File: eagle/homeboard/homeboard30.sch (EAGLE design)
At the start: 126 parts, among them IC1 XCF02S, IC2 25LC080SN, IC3 ATMEGA32U2-TQFP, Q5 BC848SMD, Q6 BC848SMD, Q7 BC848SMD, Q8 BC848SMD, T1 BSS138, T2 BC848, T3 BSS138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

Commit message: reverted changes to submitted homeboard29, moved recent changes to 29 into 30 and re-applied scart slot fix
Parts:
- C1, C3, C4, C5: value (none) -> 100nF
- C37, C38: value (none) -> 20pF
- LED1: value (none) -> 20mA
- R11, R23, R34: value (none) -> 75
- R48, R49: value (none) -> 2200
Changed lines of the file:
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@@
 <part name="Q7" library="bc548" deviceset="BC848*" device="SMD"/>
 <part name="Q8" library="bc548" deviceset="BC848*" device="SMD"/>
-<part name="R23" library="resistor" deviceset="R-EU_" device="M0805"/>
-<part name="R34" library="resistor" deviceset="R-EU_" device="M0805"/>
-<part name="C3" library="resistor" deviceset="C-EU" device="C0603"/>
-<part name="C4" library="resistor" deviceset="C-EU" device="C0603"/>
+<part name="R23" library="resistor" deviceset="R-EU_" device="M0805" value="75"/>
+<part name="R34" library="resistor" deviceset="R-EU_" device="M0805" value="75"/>
+<part name="C3" library="resistor" deviceset="C-EU" device="C0603" value="100nF"/>
+<part name="C4" library="resistor" deviceset="C-EU" device="C0603" value="100nF"/>
 <part name="U$2" library="cpcfpga" deviceset="TXO_7C" device=""/>
 <part name="REG2.5" library="cpcfpga" deviceset="NX1117" device="" value="2.5V"/>
@@
 <part name="SUPPLY5" library="supply2" deviceset="GND" device=""/>
 <part name="IC2" library="microchip" deviceset="25*" device="SN" technology="LC080"/>
-<part name="R48" library="resistor" deviceset="R-EU_" device="M0805"/>
-<part name="C1" library="resistor" deviceset="C-EU" device="C0603"/>
-<part name="C5" library="resistor" deviceset="C-EU" device="C0603"/>
-<part name="R49" library="resistor" deviceset="R-EU_" device="M0805"/>
+<part name="R48" library="resistor" deviceset="R-EU_" device="M0805" value="2200"/>
+<part name="C1" library="resistor" deviceset="C-EU" device="C0603" value="100nF"/>
+<part name="C5" library="resistor" deviceset="C-EU" device="C0603" value="100nF"/>
+<part name="R49" library="resistor" deviceset="R-EU_" device="M0805" value="2200"/>
 <part name="SUPPLY6" library="supply2" deviceset="GND" device=""/>
 <part name="SUPPLY7" library="supply2" deviceset="GND" device=""/>
@@
 <part name="SUPPLY19" library="supply2" deviceset="GND" device=""/>
 <part name="Q1" library="special" deviceset="XTAL/S" device=""/>
-<part name="C37" library="rcl" deviceset="C-EU" device="C0805"/>
-<part name="C38" library="rcl" deviceset="C-EU" device="C0805"/>
+<part name="C37" library="rcl" deviceset="C-EU" device="C0805" value="20pF"/>
+<part name="C38" library="rcl" deviceset="C-EU" device="C0805" value="20pF"/>
 <part name="SUPPLY20" library="supply2" deviceset="GND" device=""/>
 <part name="PWR_HDR" library="jumper" deviceset="JP1Q" device=""/>
@@
 <attribute name="OC_NEWARK" value="unknown"/>
 </part>
-<part name="R11" library="resistor" deviceset="R-EU_" device="M0805"/>
+<part name="R11" library="resistor" deviceset="R-EU_" device="M0805" value="75"/>
 <part name="SUPPLY17" library="supply2" deviceset="GND" device=""/>
-<part name="LED1" library="adafruit" deviceset="LED" device="CHIPLED_0805"/>
+<part name="LED1" library="adafruit" deviceset="LED" device="CHIPLED_0805" value="20mA"/>
 </parts>
 <sheets>
@@
 </segment>
 </net>
-<net name="X_CAS" class="0">
-<segment>
-<wire x1="177.8" y1="114.3" x2="162.56" y2="114.3" width="0.1524" layer="91"/>
-<label x="162.56" y="114.3" size="1.778" layer="95"/>
-</segment>
-</net>

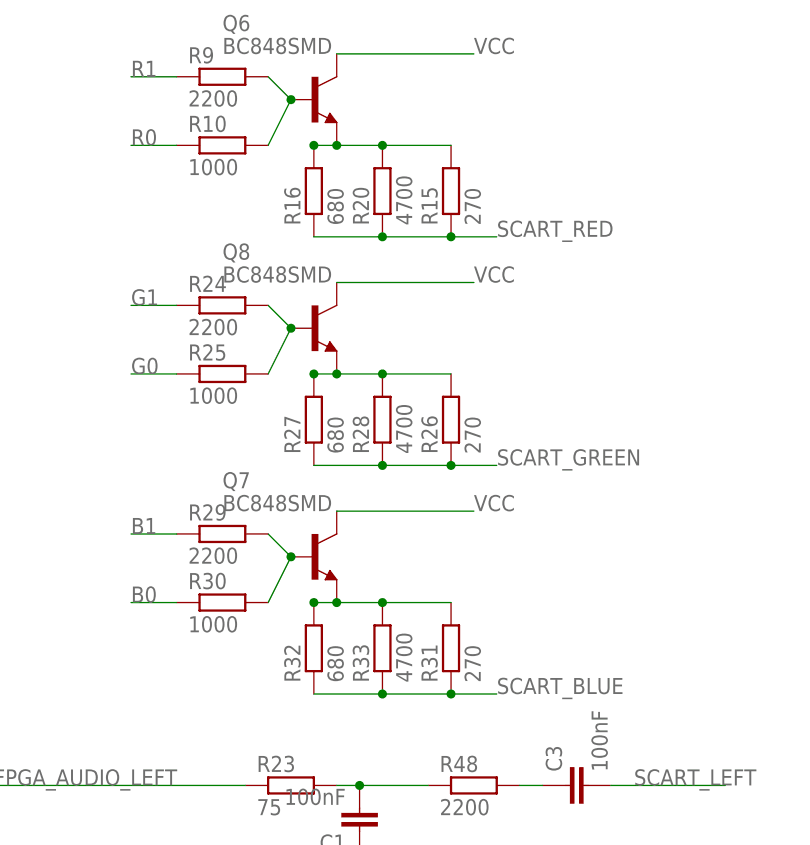
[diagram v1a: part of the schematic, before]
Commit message: replaced parallel resistors in DAC with single 180
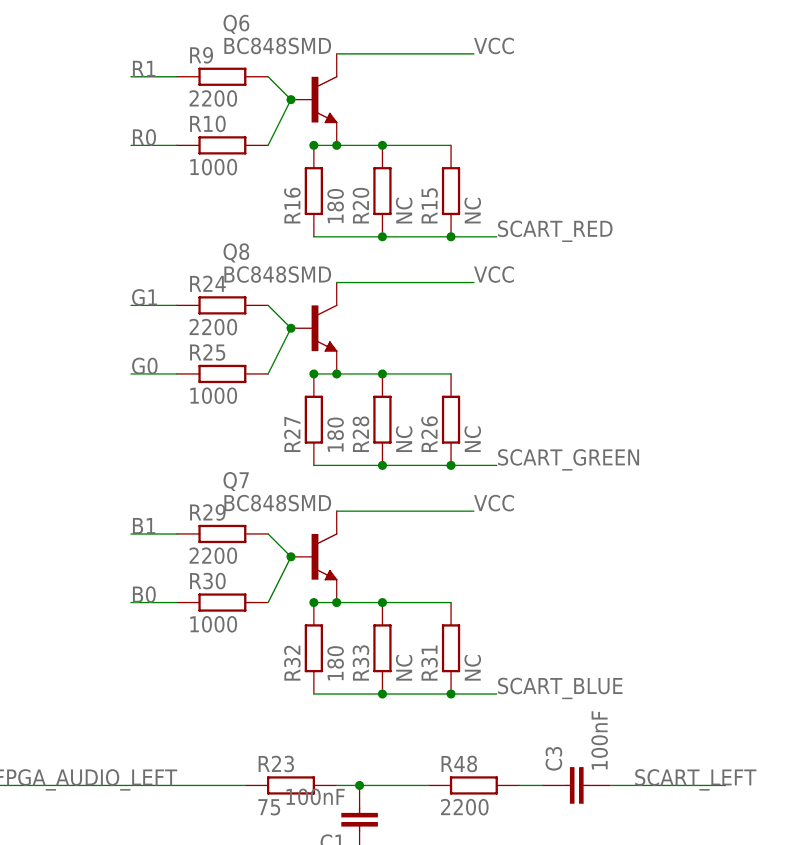
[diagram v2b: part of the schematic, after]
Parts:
- R15, R26, R31: value 270 -> NC
- R16, R27, R32: value 680 -> 180
- R20, R28, R33: value 4700 -> NC
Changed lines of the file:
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@@
 <part name="R13" library="rcl" deviceset="R-EU_" device="R0805" value="680"/>
 <part name="R14" library="rcl" deviceset="R-EU_" device="R0805" value="2200"/>
-<part name="R15" library="rcl" deviceset="R-EU_" device="R0805" value="270"/>
-<part name="R16" library="rcl" deviceset="R-EU_" device="R0805" value="680"/>
-<part name="R20" library="rcl" deviceset="R-EU_" device="R0805" value="4700"/>
+<part name="R15" library="rcl" deviceset="R-EU_" device="R0805" value="NC"/>
+<part name="R16" library="rcl" deviceset="R-EU_" device="R0805" value="180"/>
+<part name="R20" library="rcl" deviceset="R-EU_" device="R0805" value="NC"/>
 <part name="R24" library="rcl" deviceset="R-EU_" device="R0805" value="2200"/>
 <part name="R25" library="rcl" deviceset="R-EU_" device="R0805" value="1000"/>
-<part name="R26" library="rcl" deviceset="R-EU_" device="R0805" value="270"/>
-<part name="R27" library="rcl" deviceset="R-EU_" device="R0805" value="680"/>
-<part name="R28" library="rcl" deviceset="R-EU_" device="R0805" value="4700"/>
+<part name="R26" library="rcl" deviceset="R-EU_" device="R0805" value="NC"/>
+<part name="R27" library="rcl" deviceset="R-EU_" device="R0805" value="180"/>
+<part name="R28" library="rcl" deviceset="R-EU_" device="R0805" value="NC"/>
 <part name="R29" library="rcl" deviceset="R-EU_" device="R0805" value="2200"/>
 <part name="R30" library="rcl" deviceset="R-EU_" device="R0805" value="1000"/>
-<part name="R31" library="rcl" deviceset="R-EU_" device="R0805" value="270"/>
-<part name="R32" library="rcl" deviceset="R-EU_" device="R0805" value="680"/>
-<part name="R33" library="rcl" deviceset="R-EU_" device="R0805" value="4700"/>
+<part name="R31" library="rcl" deviceset="R-EU_" device="R0805" value="NC"/>
+<part name="R32" library="rcl" deviceset="R-EU_" device="R0805" value="180"/>
+<part name="R33" library="rcl" deviceset="R-EU_" device="R0805" value="NC"/>
 <part name="R17" library="rcl" deviceset="R-EU_" device="R0805" value="10000"/>
 <part name="R18" library="rcl" deviceset="R-EU_" device="R0805" value="4700"/>

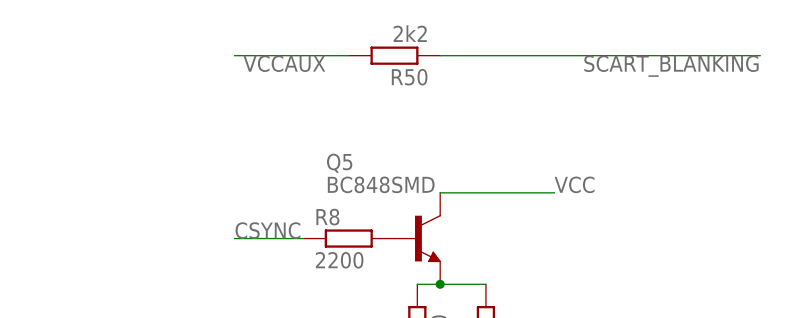
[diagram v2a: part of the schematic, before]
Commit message: scart fast blanking needs 0R link instead of 2k2 to get valid voltage
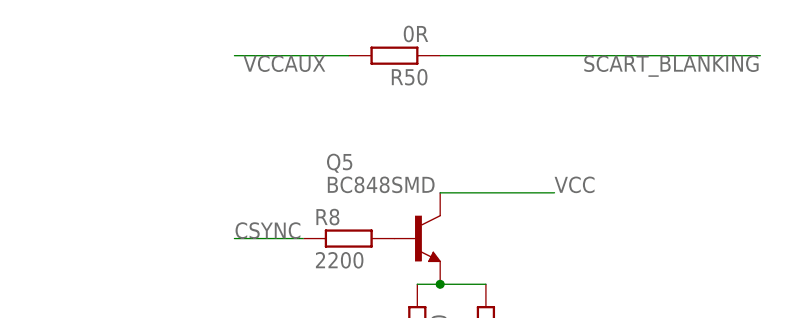
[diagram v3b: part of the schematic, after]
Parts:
- R50: value 2k2 -> 0R
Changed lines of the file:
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@@
 <part name="SUPPLY6" library="supply2" deviceset="GND" device=""/>
 <part name="SUPPLY7" library="supply2" deviceset="GND" device=""/>
-<part name="R50" library="resistor" deviceset="R-EU_" device="M0805" value="2k2"/>
+<part name="R50" library="resistor" deviceset="R-EU_" device="M0805" value="0R"/>
 <part name="IC3" library="adafruit" deviceset="ATMEGA32U2" device="-TQFP"/>
 <part name="REG3.3" library="cpcfpga" deviceset="NX1117" device="" value="3.3V"/>

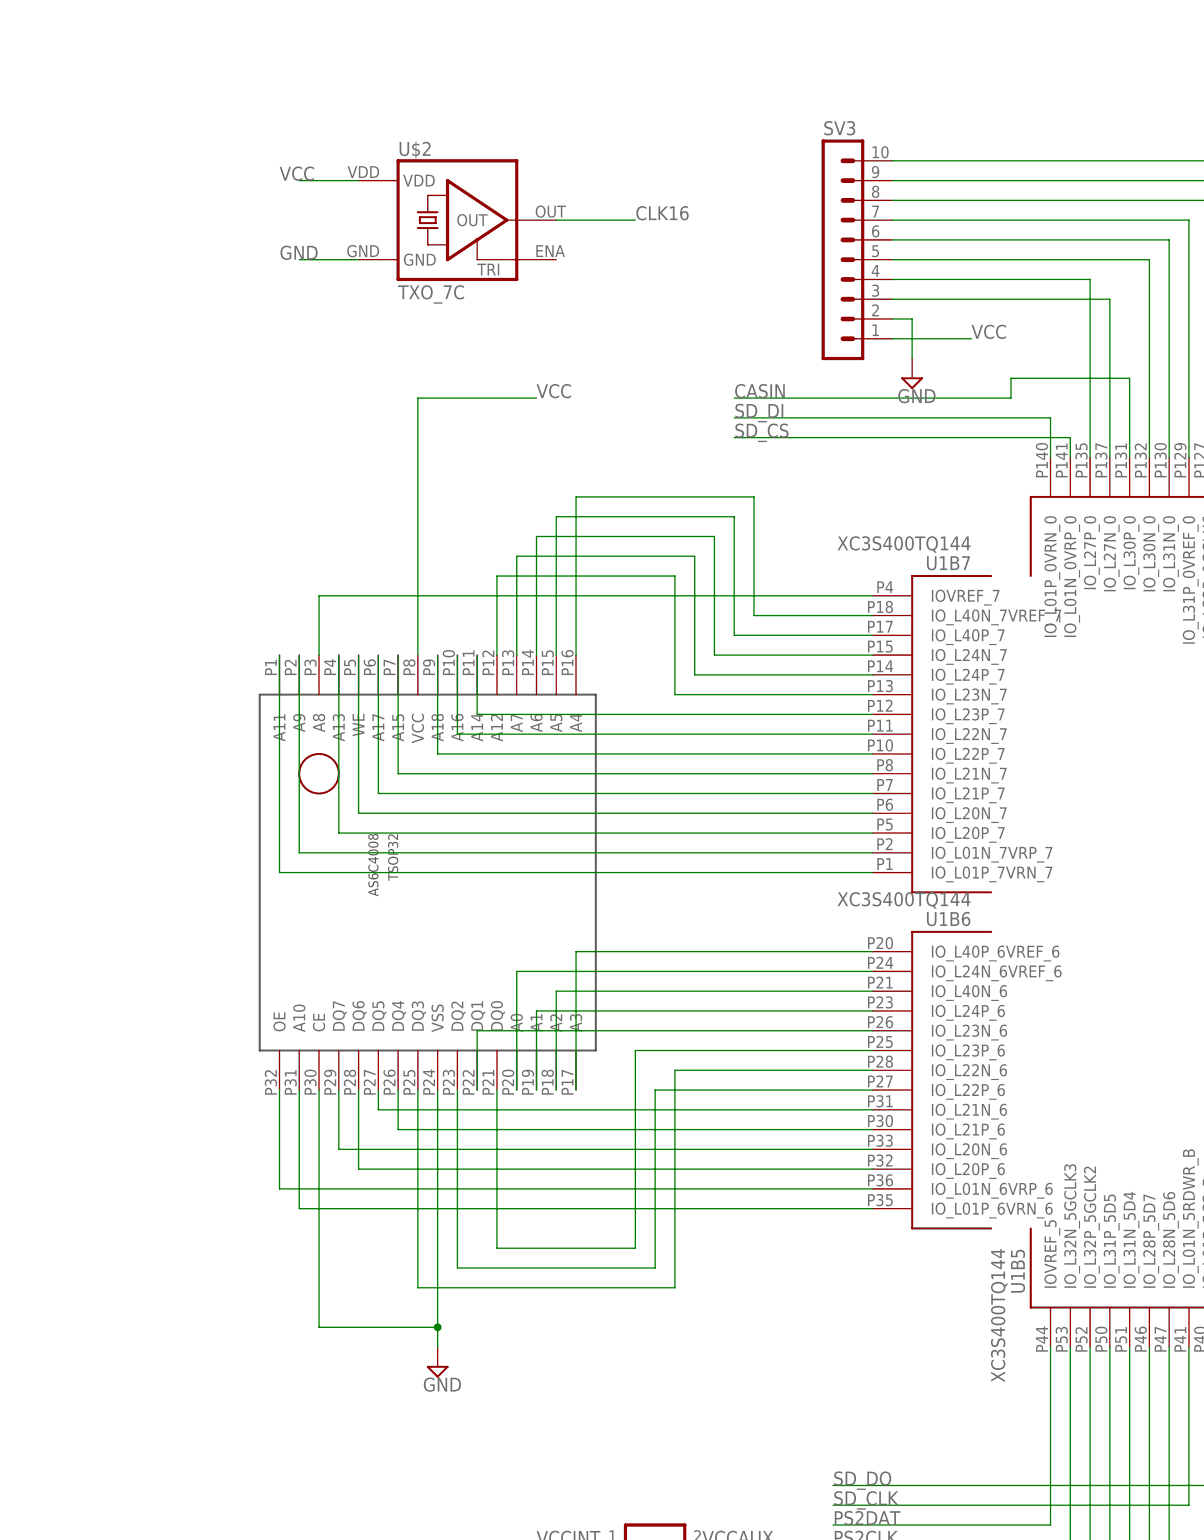
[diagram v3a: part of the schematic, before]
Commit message: name anonymous nets on sram and gpio
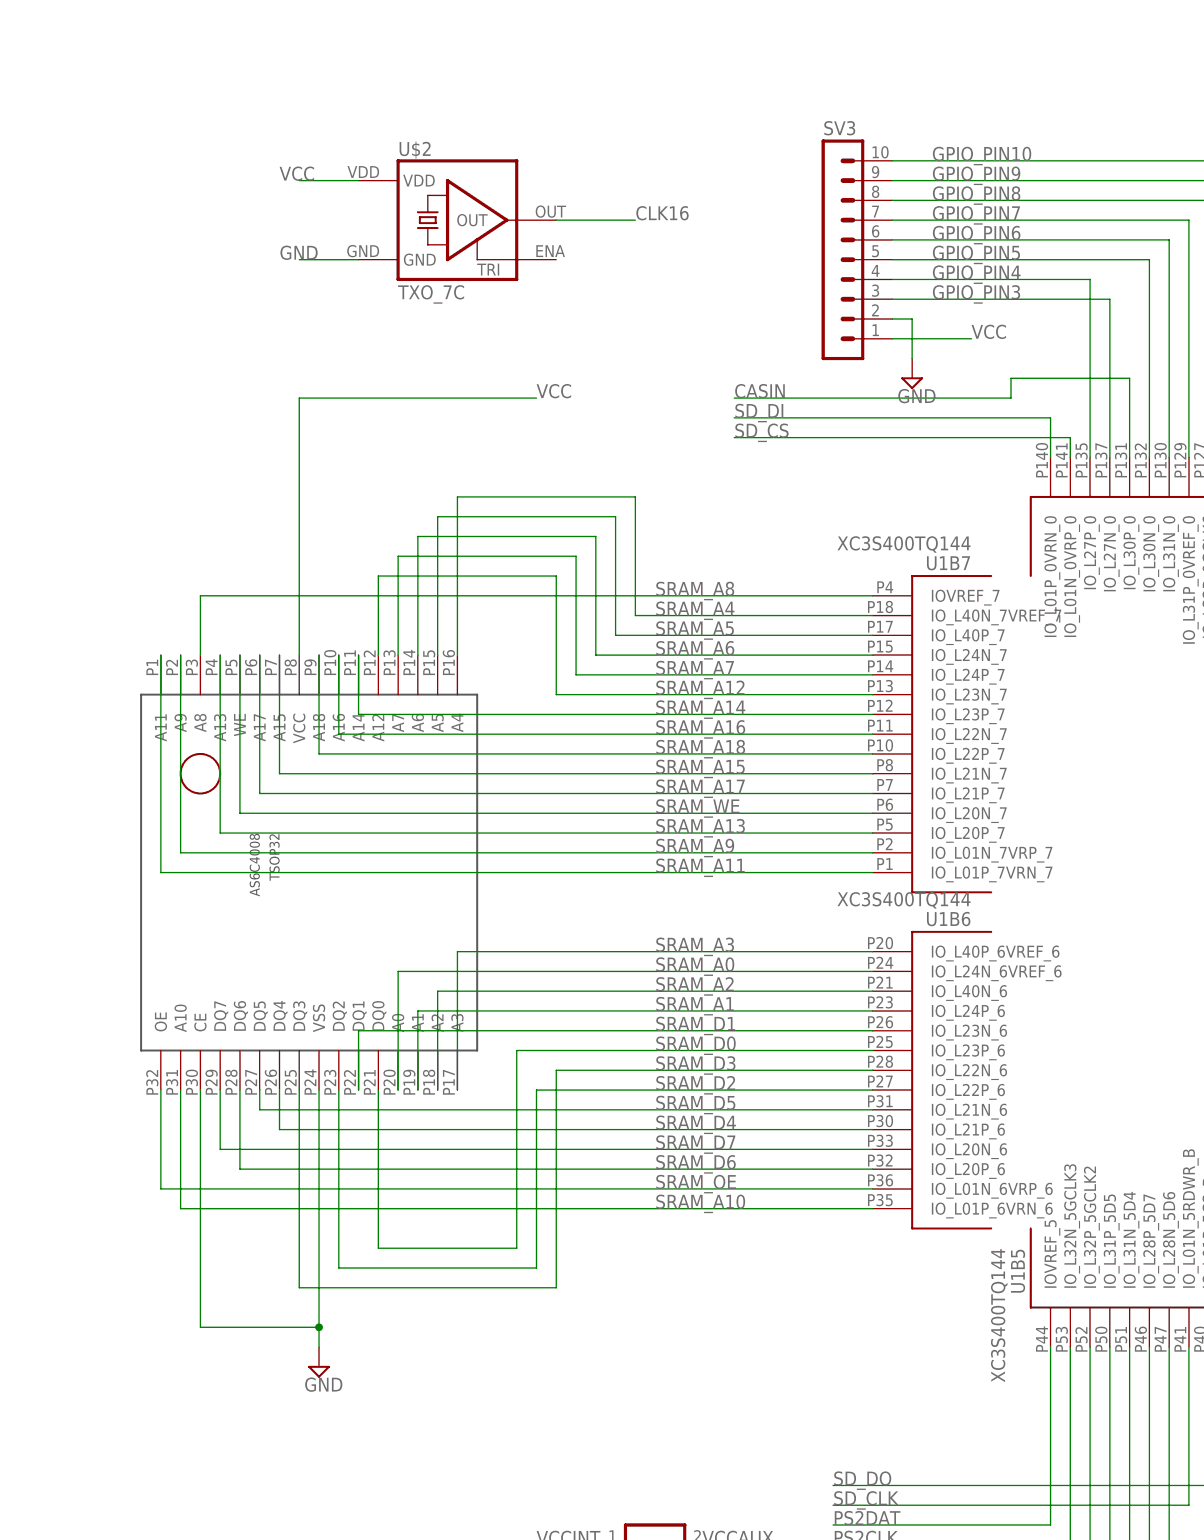
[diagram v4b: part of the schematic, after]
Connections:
- net N$1 renamed GPIO_PIN4
- net N$16 renamed GPIO_PIN10
- net N$2 renamed GPIO_PIN5
- net N$3 renamed GPIO_PIN3
- net N$4 renamed GPIO_PIN6
- net N$5 renamed GPIO_PIN7
- net N$6 renamed GPIO_PIN9
- net N$67 renamed SRAM_A11
- net N$7 renamed GPIO_PIN8
- net N$71 renamed SRAM_A9
- net N$72 renamed SRAM_A8
- net N$73 renamed SRAM_A13
- net N$74 renamed SRAM_WE
- net N$75 renamed SRAM_A17
- net N$76 renamed SRAM_A15
- net N$77 renamed SRAM_A18
- net N$78 renamed SRAM_A16
- net N$79 renamed SRAM_A14
- net N$80 renamed SRAM_A12
- net N$81 renamed SRAM_A7
- net N$82 renamed SRAM_A6
- net N$83 renamed SRAM_A5
- net N$84 renamed SRAM_A4
- net N$85 renamed SRAM_A3
- net N$86 renamed SRAM_A2
- net N$87 renamed SRAM_A1
- net N$88 renamed SRAM_A0
- net N$89 renamed SRAM_D0
- net N$90 renamed SRAM_D1
- net N$91 renamed SRAM_D2
- net N$92 renamed SRAM_D3
- net N$93 renamed SRAM_D4
- net N$94 renamed SRAM_D5
- net N$95 renamed SRAM_D6
- net N$96 renamed SRAM_D7
- net N$97 renamed SRAM_A10
- net N$98 renamed SRAM_OE
